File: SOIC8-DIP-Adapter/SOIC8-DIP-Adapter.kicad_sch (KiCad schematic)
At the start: 3 parts, among them J1 01-04, J2 05-08, U1 SOIC-8

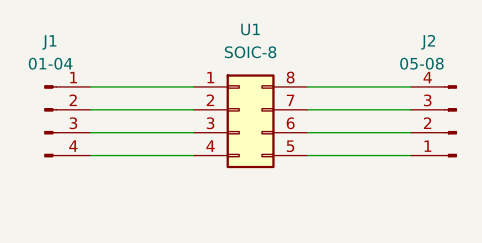
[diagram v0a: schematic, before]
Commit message: Finish SOIC-8 adapter
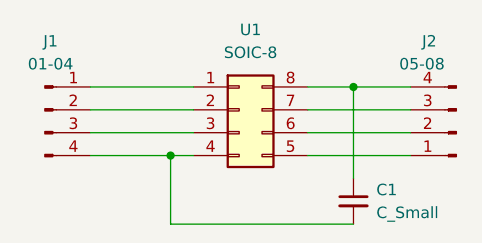
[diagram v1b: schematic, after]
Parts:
- added C1: C_Small, Capacitor_SMD:C_0603_1608Metric, symbol Device:C_Small
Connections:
- net at J2.4 (Pin_4), U1.8 (Pin_8): now also C1.1
- net at J1.4 (Pin_4), U1.4 (Pin_4): now also C1.2
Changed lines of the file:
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@@
 (kicad_sch (version 20211123) (generator eeschema)
   (paper "A4")
+  (junction (at 132.08 77.47) (diameter 0) (color 0 0 0 0)
+  )
+  (junction (at 152.4 69.85) (diameter 0) (color 0 0 0 0)
+  )
   (wire (pts (xy 123.19 69.85) (xy 134.62 69.85))
     (stroke (width 0) (type default) (color 0 0 0 0))
   )
-  (wire (pts (xy 147.32 69.85) (xy 158.75 69.85))
+  (wire (pts (xy 147.32 69.85) (xy 152.4 69.85))
     (stroke (width 0) (type default) (color 0 0 0 0))
   )
@@
     (stroke (width 0) (type default) (color 0 0 0 0))
   )
+  (wire (pts (xy 132.08 77.47) (xy 134.62 77.47))
+    (stroke (width 0) (type default) (color 0 0 0 0))
+  )
+  (wire (pts (xy 132.08 85.09) (xy 132.08 77.47))
+    (stroke (width 0) (type default) (color 0 0 0 0))
+  )
   (wire (pts (xy 147.32 74.93) (xy 158.75 74.93))
+    (stroke (width 0) (type default) (color 0 0 0 0))
+  )
+  (wire (pts (xy 152.4 85.09) (xy 132.08 85.09))
+    (stroke (width 0) (type default) (color 0 0 0 0))
+  )
+  (wire (pts (xy 152.4 69.85) (xy 152.4 80.01))
     (stroke (width 0) (type default) (color 0 0 0 0))
   )
@@
     (stroke (width 0) (type default) (color 0 0 0 0))
   )
+  (wire (pts (xy 152.4 69.85) (xy 158.75 69.85))
+    (stroke (width 0) (type default) (color 0 0 0 0))
+  )
   (wire (pts (xy 123.19 72.39) (xy 134.62 72.39))
     (stroke (width 0) (type default) (color 0 0 0 0))
   )
-  (wire (pts (xy 123.19 77.47) (xy 134.62 77.47))
+  (wire (pts (xy 123.19 77.47) (xy 132.08 77.47))
     (stroke (width 0) (type default) (color 0 0 0 0))
   )
@@
     (pin "3")
     (pin "4")
+  )
+  (symbol (lib_id "Device:C_Small") (at 152.4 82.55 0) (unit 1)
+    (in_bom yes) (on_board yes) (fields_autoplaced)
+    (property "Reference" "C1" (id 0) (at 154.94 81.2862 0)
+      (effects (font (size 1.27 1.27)) (justify left))
+    )
+    (property "Value" "C_Small" (id 1) (at 154.94 83.8262 0)
+      (effects (font (size 1.27 1.27)) (justify left))
+    )
+    (property "Footprint" "Capacitor_SMD:C_0603_1608Metric" (id 2) (at 152.4 82.55 0)
+      (effects (font (size 1.27 1.27)) hide)
+    )
+    (property "Datasheet" "~" (id 3) (at 152.4 82.55 0)
+      (effects (font (size 1.27 1.27)) hide)
+    )
+    (pin "1")
+    (pin "2")
   )
   (symbol (lib_id "Connector:Conn_01x04_Male") (at 118.11 72.39 0) (unit 1)
@@
   )
   (symbol_instances
+    (path "/5084ee35-285e-4383-9f19-548c8d24e8b5"
+      (reference "C1") (unit 1) (value "C_Small") (footprint "Capacitor_SMD:C_0603_1608Metric")
+    )
     (path "/6ddd76a4-62b8-4b53-b884-3aa943b4f260"
       (reference "J1") (unit 1) (value "01-04") (footprint "SOIC8-DIP-Adapter:PinHeader_1x04_P2.54mm_Vertical_NoSilkscreen")
